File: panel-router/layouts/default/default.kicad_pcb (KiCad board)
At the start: 2 copper layers, 18.5 x 90 mm, 4 parts

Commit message: Cleanup
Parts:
- moved 15V-25V DC 19.8 mm to (93.0, 96.5), turned to 90 degrees
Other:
- outline, holes or cut-outs redrawn
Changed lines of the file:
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@@
 	(footprint "CUI_PJ_002BH:DC-IN-TH_PJ-002BH"
 		(layer "B.Cu")
-		(at 92.2048 116.2436)
+		(at 92.9525 96.495 90)
 		(property "Reference" "15V-25V DC"
-			(at 10.1572 4.4064 180)
-			(layer "B.SilkS")
-			(effects
-				(font
-					(size 1 1)
-					(thickness 0.15)
-				)
-				(justify left mirror)
+			(at 5.995 4.5475 90)
+			(layer "B.SilkS")
+			(effects
+				(font
+					(size 1 1)
+					(thickness 0.15)
+				)
+				(justify mirror)
 			)
 		)
 		(property "Value" ""
-			(at 0 -6.35 0)
+			(at 0 -6.35 90)
 			(layer "B.Fab")
 			(effects
@@
 		)
 		(property "Datasheet" "https://www.lcsc.com/datasheet/lcsc_datasheet_2409302136_CUI-PJ-002BH_C22359705.pdf"
-			(at 0 0 0)
+			(at 0 0 90)
 			(layer "User.9")
 			(hide yes)
@@
 		)
 		(property "Description" ""
-			(at 0 0 0)
+			(at 0 0 90)
 			(layer "B.Fab")
 			(hide yes)
@@
 		)
 		(property "LCSC" "C22359705"
-			(at 0 0 0)
+			(at 0 0 90)
 			(layer "User.9")
 			(hide yes)
@@
 		)
 		(property "Manufacturer" "CUI"
-			(at 0 0 0)
+			(at 0 0 90)
 			(layer "User.9")
 			(hide yes)
@@
 		)
 		(property "Partnumber" "PJ-002BH"
-			(at 0 0 0)
+			(at 0 0 90)
 			(layer "User.9")
 			(hide yes)
@@
 		)
 		(property "atopile_address" "dc_input"
-			(at 0 0 0)
+			(at 0 0 90)
 			(layer "User.9")
 			(hide yes)
@@
 		)
 		(property "lcsc_id" "C22359705"
-			(at 0 0 0)
+			(at 0 0 90)
 			(layer "User.9")
 			(hide yes)
@@
 		)
 		(attr through_hole)
+		(fp_line
+			(start 10.8 -6.98)
+			(end 10.8 2.29)
+			(stroke
+				(width 0.25)
+				(type solid)
+			)
+			(layer "B.SilkS")
+		)
 		(fp_line
 			(start -3.81 -6.98)
@@
 		)
 		(fp_line
+			(start 10.8 2.29)
+			(end 2.12 2.29)
+			(stroke
+				(width 0.25)
+				(type solid)
+			)
+			(layer "B.SilkS")
+		)
+		(fp_line
+			(start -2.12 2.29)
+			(end -3.81 2.29)
+			(stroke
+				(width 0.25)
+				(type solid)
+			)
+			(layer "B.SilkS")
+		)
+		(fp_line
 			(start -3.81 2.29)
 			(end -3.81 -0.33)
-			(stroke
-				(width 0.25)
-				(type solid)
-			)
-			(layer "B.SilkS")
-		)
-		(fp_line
-			(start -2.12 2.29)
-			(end -3.81 2.29)
-			(stroke
-				(width 0.25)
-				(type solid)
-			)
-			(layer "B.SilkS")
-		)
-		(fp_line
-			(start 10.8 -6.98)
-			(end 10.8 2.29)
-			(stroke
-				(width 0.25)
-				(type solid)
-			)
-			(layer "B.SilkS")
-		)
-		(fp_line
-			(start 10.8 2.29)
-			(end 2.12 2.29)
 			(stroke
 				(width 0.25)
@@
 		)
 		(pad "1" thru_hole oval
-			(at -3 -2.35)
+			(at -3 -2.35 90)
 			(size 1.7 4.3)
 			(drill oval 0.999998 3.499993)
@@
 		)
 		(pad "2" thru_hole oval
-			(at 3 -2.35)
+			(at 3 -2.35 90)
 			(size 1.7 3.8)
 			(drill oval 0.999998 2.999994)
@@
 		)
 		(pad "3" thru_hole oval
-			(at 0 2.35)
+			(at 0 2.35 90)
 			(size 3.8 1.7)
 			(drill oval 2.999994 0.999998)
@@
 		)
 	)
+	(gr_circle
+		(center 101.5 87)
+		(end 102.75 87)
+		(stroke
+			(width 0.05)
+			(type solid)
+		)
+		(fill no)
+		(layer "Edge.Cuts")
+	)
+	(gr_circle
+		(center 101.5 117)
+		(end 102.75 117)
+		(stroke
+			(width 0.05)
+			(type solid)
+		)
+		(fill no)
+		(layer "Edge.Cuts")
+	)
+	(gr_circle
+		(center 101.5 143)
+		(end 102.75 143)
+		(stroke
+			(width 0.05)
+			(type solid)
+		)
+		(fill no)
+		(layer "Edge.Cuts")
+	)
+	(gr_circle
+		(center 101.5 113)
+		(end 102.75 113)
+		(stroke
+			(width 0.05)
+			(type solid)
+		)
+		(fill no)
+		(layer "Edge.Cuts")
+	)
 	(gr_rect
 		(start 85 85)
@@
 		(stroke
 			(width 0.05)
+			(type solid)
+		)
+		(fill no)
+		(layer "Edge.Cuts")
+	)
+	(gr_circle
+		(center 101.5 173)
+		(end 102.75 173)
+		(stroke
+			(width 0.05)
+			(type solid)
+		)
+		(fill no)
+		(layer "Edge.Cuts")
+	)
+	(gr_circle
+		(center 101.5 147)
+		(end 102.75 147)
+		(stroke
+			(width 0.05)

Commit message: PoE Improvements
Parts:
- moved + H3 - 4.00 mm to (100.0, 164.0)
- moved 15V-25V DC 2.36 mm to (90.6, 96.4)
- moved + H2 - 2.00 mm to (100.0, 132.0)
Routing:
- net GND: track 0.00 -> 5.08 mm
- net V+: track 5.08 -> 7.62 mm
- net 4: track 75.9 -> 78.2 mm
- net 3: track 81.9 -> 83.2 mm
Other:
- board size 18.5 x 90 mm -> 21 x 94 mm
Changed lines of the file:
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@@
 	(footprint "BOOMELE_2_54_2_3P:HDR-TH_6P-P2.54-V-M-R2-C3-S2.54-1"
 		(layer "F.Cu")
-		(at 100 130 90)
+		(at 100 132 90)
 		(property "Reference" "+ H2 -"
 			(at 0 -4 90)
@@
 	(footprint "BOOMELE_2_54_2_3P:HDR-TH_6P-P2.54-V-M-R2-C3-S2.54-1"
 		(layer "F.Cu")
-		(at 100 160 90)
+		(at 100 164 90)
 		(property "Reference" "+ H3 -"
 			(at 0 -4 90)
@@
 	(footprint "CUI_PJ_002BH:DC-IN-TH_PJ-002BH"
 		(layer "B.Cu")
-		(at 92.9525 96.495 90)
+		(at 90.5896 96.4212 90)
 		(property "Reference" "15V-25V DC"
 			(at 5.995 4.5475 90)
@@
 	)
 	(gr_circle
-		(center 101.5 117)
-		(end 102.75 117)
+		(center 101.5 119)
+		(end 102.75 119)
 		(stroke
 			(width 0.05)
@@
 	)
 	(gr_circle
-		(center 101.5 143)
-		(end 102.75 143)
+		(center 101.5 145)
+		(end 102.75 145)
 		(stroke
 			(width 0.05)
@@
 	)
 	(gr_rect
-		(start 85 85)
-		(end 103.5 175)
+		(start 82.5 85)
+		(end 103.5 179)
 		(stroke
 			(width 0.05)
@@
 	)
 	(gr_circle
-		(center 101.5 173)
-		(end 102.75 173)
+		(center 101.5 177)
+		(end 102.75 177)
 		(stroke
 			(width 0.05)
@@
 	)
 	(gr_circle
-		(center 101.5 147)
-		(end 102.75 147)
+		(center 101.5 151)
+		(end 102.75 151)
 		(stroke
 			(width 0.05)
@@
 	)
 	(segment
-		(start 98.73 162.54)
-		(end 101.27 162.54)
-		(width 0.4)
-		(layer "F.Cu")
+		(start 98.73 161.46)
+		(end 101.27 161.46)
+		(width 0.5)
+		(layer "F.Cu")
+		(net 1)
+	)
+	(segment
+		(start 98.73 97.46)
+		(end 101.27 97.46)
+		(width 0.5)
+		(layer "F.Cu")
+		(net 1)
+	)
+	(segment
+		(start 101.27 102.54)
+		(end 98.73 102.54)
+		(width 0.5)
+		(layer "B.Cu")
 		(net 2)
 	)
 	(segment
-		(start 98.73 132.54)
-		(end 101.27 132.54)
-		(width 0.4)
-		(layer "F.Cu")
+		(start 98.73 134.54)
+		(end 101.27 134.54)
+		(width 0.5)
+		(layer "B.Cu")
 		(net 2)
 	)
 	(segment
-		(start 92.9132 128.7272)
-		(end 92.8116 128.6256)
-		(width 0.2)
-		(layer "F.Cu")
-		(net 3)
-	)
-	(segment
-		(start 96.4184 158.6992)
-		(end 99.9692 158.6992)
-		(width 0.2)
-		(layer "F.Cu")
-		(net 3)
-	)
-	(segment
-		(start 101.1964 130)
-		(end 99.9236 128.7272)
+		(start 98.73 166.54)
+		(end 101.27 166.54)
+		(width 0.5)
+		(layer "B.Cu")
+		(net 2)
+	)
+	(segment
+		(start 92.8116 128.6256)
+		(end 92.8116 124.5108)
+		(width 0.2)
+		(layer "F.Cu")
+		(net 3)
+	)
+	(segment
+		(start 97.536 162.7632)
+		(end 100.0332 162.7632)
 		(width 0.2)
 		(layer "F.Cu")
@@
 	)
 	(segment
+		(start 92.8116 124.5108)
+		(end 98.9584 118.364)
+		(width 0.2)
+		(layer "F.Cu")
+		(net 3)
+	)
+	(segment
+		(start 100.0292 130.7592)
+		(end 101.27 132)
+		(width 0.2)
+		(layer "F.Cu")
+		(net 3)
+	)
+	(segment
+		(start 94.8944 130.7592)
+		(end 94.7928 130.6576)
+		(width 0.2)
+		(layer "F.Cu")
+		(net 3)
+	)
+	(segment
+		(start 95.8596 161.0868)
+		(end 97.536 162.7632)
+		(width 0.2)
+		(layer "F.Cu")
+		(net 3)
+	)
+	(segment
+		(start 100.0332 162.7632)
+		(end 101.27 164)
+		(width 0.2)
+		(layer "F.Cu")
+		(net 3)
+	)
+	(segment
+		(start 94.7928 130.6576)
+		(end 94.7928 130.6068)
+		(width 0.2)
+		(layer "F.Cu")
+		(net 3)
+	)
+	(segment
 		(start 95.8596 149.352)
-		(end 95.8596 158.1404)
-		(width 0.2)
-		(layer "F.Cu")
-		(net 3)
-	)
-	(segment
-		(start 101.27 130)
-		(end 101.1964 130)
+		(end 95.8596 161.0868)
+		(width 0.2)
+		(layer "F.Cu")
+		(net 3)
+	)
+	(segment
+		(start 94.8944 130.7592)
+		(end 100.0292 130.7592)
 		(width 0.2)
 		(layer "F.Cu")
@@
 	)
 	(segment
-		(start 99.9692 158.6992)
-		(end 101.27 160)
-		(width 0.2)
-		(layer "F.Cu")
-		(net 3)
-	)
-	(segment
-		(start 95.8596 158.1404)
-		(end 96.4184 158.6992)
-		(width 0.2)
-		(layer "F.Cu")
-		(net 3)
-	)
-	(segment
-		(start 99.9236 128.7272)
-		(end 92.9132 128.7272)
-		(width 0.2)
-		(layer "F.Cu")
-		(net 3)
-	)
-	(segment
-		(start 92.8116 124.5108)
-		(end 98.9584 118.364)
-		(width 0.2)
-		(layer "F.Cu")
-		(net 3)
-	)
-	(segment
-		(start 92.8116 128.6256)
-		(end 92.8116 124.5108)
+		(start 94.7928 130.6068)
+		(end 92.8116 128.6256)
 		(width 0.2)
 		(layer "F.Cu")
@@
 	)
 	(via
-		(at 92.8116 128.6256)
+		(at 94.8944 130.7592)
 		(size 0.6)
 		(drill 0.3)
@@
 	)
 	(segment
+		(start 94.7928 148.2852)
+		(end 95.8596 149.352)
+		(width 0.2)
+		(layer "B.Cu")
+		(net 3)
+	)
+	(segment
 		(start 100.0256 101.2444)
 		(end 101.27 100)
@@
 	)
 	(segment
-		(start 94.7928 148.2852)
-		(end 95.8596 149.352)
-		(width 0.2)
-		(layer "B.Cu")
-		(net 3)
-	)
-	(segment
 		(start 96.4184 101.9556)
 		(end 97.1296 101.2444)
@@
 	)
 	(segment
-		(start 94.7928 130.6068)
-		(end 94.7928 148.2852)
+		(start 94.8944 130.7592)
+		(end 94.7928 130.8608)
 		(width 0.2)
 		(layer "B.Cu")
@@
 	)
 	(segment
-		(start 92.8116 128.6256)
-		(end 94.7928 130.6068)
-		(width 0.2)
-		(layer "B.Cu")
-		(net 3)
-	)
-	(segment
-		(start 96.012 159.1056)
-		(end 97.8356 159.1056)
+		(start 94.7928 130.8608)
+		(end 94.7928 148.2852)
+		(width 0.2)
+		(layer "B.Cu")
+		(net 3)
+	)
+	(segment
+		(start 92.1004 124.0536)
+		(end 98.1964 117.9576)
+		(width 0.2)
+		(layer "F.Cu")
+		(net 4)
+	)
+	(segment
+		(start 98.3528 131.6228)
+		(end 98.73 132)
 		(width 0.2)
 		(layer "F.Cu")
@@
 	(segment
 		(start 95.1484 149.5552)
-		(end 95.1484 158.242)
-		(width 0.2)
-		(layer "F.Cu")
-		(net 4)
-	)
-	(segment
-		(start 97.8356 159.1056)
-		(end 98.73 160)
+		(end 95.1484 162.1536)
+		(width 0.2)
+		(layer "F.Cu")
+		(net 4)
+	)
+	(segment
+		(start 94.0308 131.6228)
+		(end 92.1004 129.6924)
+		(width 0.2)
+		(layer "F.Cu")
+		(net 4)
+	)
+	(segment
+		(start 94.0308 148.4376)
+		(end 95.1484 149.5552)
+		(width 0.2)
+		(layer "F.Cu")
+		(net 4)
+	)
+	(segment
+		(start 98.1964 117.9576)
+		(end 98.1964 109.5248)
+		(width 0.2)
+		(layer "F.Cu")
+		(net 4)
+	)
+	(segment
+		(start 96.9948 164)
+		(end 98.73 164)
+		(width 0.2)
+		(layer "F.Cu")
+		(net 4)
+	)
+	(segment
+		(start 94.0308 131.6228)
+		(end 98.3528 131.6228)
+		(width 0.2)
+		(layer "F.Cu")
+		(net 4)
+	)
+	(segment
+		(start 95.1484 162.1536)
+		(end 96.9948 164)
 		(width 0.2)
 		(layer "F.Cu")
@@
 		(net 4)
 	)
-	(segment
-		(start 92.254 129.846)
-		(end 92.408 130)
-		(width 0.2)
-		(layer "F.Cu")
-		(net 4)
-	)
-	(segment
-		(start 98.1964 117.9576)
-		(end 98.1964 109.5248)
-		(width 0.2)
-		(layer "F.Cu")
-		(net 4)
-	)
-	(segment
-		(start 92.408 130)
-		(end 98.73 130)
-		(width 0.2)
-		(layer "F.Cu")
-		(net 4)
-	)
-	(segment
-		(start 92.1004 124.0536)
-		(end 98.1964 117.9576)
-		(width 0.2)
-		(layer "F.Cu")
-		(net 4)
-	)
-	(segment
-		(start 92.254 129.846)
-		(end 92.1004 129.6924)
-		(width 0.2)
-		(layer "F.Cu")
-		(net 4)
-	)
-	(segment
-		(start 95.1484 158.242)
-		(end 96.012 159.1056)
-		(width 0.2)
-		(layer "F.Cu")
-		(net 4)
-	)
-	(segment
-		(start 94.0308 148.4376)
-		(end 95.1484 149.5552)
-		(width 0.2)
-		(layer "F.Cu")
-		(net 4)
-	)
 	(via
-		(at 92.254 129.846)
+		(at 94.0308 131.6228)
 		(size 0.6)
 		(drill 0.3)
@@
 	)
 	(segment
-		(start 92.254 129.846)
-		(end 94.0308 131.6228)
+		(start 98.1964 108.1024)
+		(end 95.8088 105.7148)
 		(width 0.2)
 		(layer "B.Cu")
@@
 		(start 94.0308 131.6228)
 		(end 94.0308 148.4376)
-		(width 0.2)
-		(layer "B.Cu")
-		(net 4)
-	)
-	(segment
-		(start 98.1964 108.1024)
-		(end 95.8088 105.7148)
 		(width 0.2)
 		(layer "B.Cu")
@@
 		(polygon
 			(pts
-				(xy 76.1524 80.9364) (xy 111.1524 80.9364) (xy 110.5936 177.6708) (xy 75.5936 177.6708)
+				(xy 76.1524 80.9364) (xy 111.1524 80.9364) (xy 110.7968 180.5664) (xy 75.7968 180.5664)
 			)
 		)
@@
 		(polygon
 			(pts
-				(xy 80.7112 83.330902) (xy 115.7112 83.330902) (xy 115.6096 178.846102) (xy 80.6096 178.846102)
-			)
-		)
+				(xy 80.7112 83.330902) (xy 115.7112 83.330902) (xy 115.7112 182.249702) (xy 80.7112 182.249702)
+			)
+		)

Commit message: Header & Silkscreen Updates
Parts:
- H1: renamed from + H1 -
- H2: renamed from + H2 -
- H3: renamed from + H3 -
- moved H1 15.5 mm to (96.0, 115.0), turned to -90 degrees
- moved H2 15.5 mm to (96.0, 147.0), turned to -90 degrees
- moved H3 15.5 mm to (96.0, 179.0), turned to -90 degrees
- moved 15V-25V DC 15.4 mm to (87.1, 111.4)
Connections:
- H1 pad 2: V+ -> GND
- H1 pad 5: GND -> V+
- H2 pad 2: V+ -> GND
- H2 pad 5: GND -> V+
- H3 pad 2: V+ -> GND
- H3 pad 5: GND -> V+
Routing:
- net V+: track 7.62 -> 0.00 mm
- net 4: track 78.2 -> 83.8 mm
- net GND: track 5.08 -> 0.00 mm
- net 3: track 83.2 -> 78.2 mm

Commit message: Basic layout tweaks
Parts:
- moved H3 2.00 mm to (96.0, 177.0)
- moved H2 1.00 mm to (96.0, 146.0)
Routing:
- net 4: track 83.8 -> 81.3 mm
- net 3: track 78.2 -> 77.2 mm
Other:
- board size 21 x 94 mm -> 21 x 92 mm
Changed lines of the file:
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@@
 	(footprint "BOOMELE_2_54_2_3P:HDR-TH_6P-P2.54-V-M-R2-C3-S2.54-1"
 		(layer "F.Cu")
-		(at 96 147 -90)
+		(at 96 146 -90)
 		(property "Reference" "H2"
 			(at 0 3.5 90)
@@
 	(footprint "BOOMELE_2_54_2_3P:HDR-TH_6P-P2.54-V-M-R2-C3-S2.54-1"
 		(layer "F.Cu")
-		(at 96 179 -90)
+		(at 96 177 -90)
 		(property "Reference" "H3"
 			(at 0 3.5 90)
@@
 	)
 	(gr_circle
-		(center 98 134)
-		(end 99.25 134)
+		(center 98 133)
+		(end 99.25 133)
 		(stroke
 			(width 0.05)
@@
 	)
 	(gr_circle
-		(center 98 160)
-		(end 99.25 160)
+		(center 98 159)
+		(end 99.25 159)
 		(stroke
 			(width 0.05)
@@
 	(gr_rect
 		(start 79 100)
-		(end 100 194)
+		(end 100 192)
 		(stroke
 			(width 0.05)
@@
 	)
 	(gr_circle
-		(center 98 192)
-		(end 99.25 192)
+		(center 98 190)
+		(end 99.25 190)
 		(stroke
 			(width 0.05)
@@
 	)
 	(gr_circle
-		(center 98 166)
-		(end 99.25 166)
+		(center 98 164)
+		(end 99.25 164)
 		(stroke
 			(width 0.05)
@@
 	)
 	(segment
-		(start 94.8528 146.6228)
-		(end 95.23 147)
-		(width 0.2)
-		(layer "F.Cu")
-		(net 1)
-	)
-	(segment
 		(start 90.5308 146.6228)
 		(end 88.6004 144.6924)
@@
 	)
 	(segment
+		(start 94.73 177)
+		(end 95.23 177.5)
+		(width 0.2)
+		(layer "F.Cu")
+		(net 1)
+	)
+	(segment
 		(start 90.5764 163.4832)
 		(end 90.5764 176.0816)
@@
 	)
 	(segment
+		(start 90.5308 146.6228)
+		(end 90.6536 146.5)
+		(width 0.2)
+		(layer "F.Cu")
+		(net 1)
+	)
+	(segment
+		(start 94.6964 132.9576)
+		(end 94.6964 124.5248)
+		(width 0.2)
+		(layer "F.Cu")
+		(net 1)
+	)
+	(segment
+		(start 94.23 146.5)
+		(end 94.73 146)
+		(width 0.2)
+		(layer "F.Cu")
+		(net 1)
+	)
+	(segment
 		(start 90.5308 163.4376)
 		(end 90.5764 163.4832)
@@
 	)
 	(segment
-		(start 94.6964 132.9576)
-		(end 94.6964 124.5248)
-		(width 0.2)
-		(layer "F.Cu")
-		(net 1)
-	)
-	(segment
-		(start 93.4948 179)
-		(end 95.23 179)
-		(width 0.2)
-		(layer "F.Cu")
-		(net 1)
-	)
-	(segment
-		(start 90.5308 146.6228)
-		(end 94.8528 146.6228)
-		(width 0.2)
-		(layer "F.Cu")
-		(net 1)
-	)
-	(segment
 		(start 90.5764 176.0816)
-		(end 93.4948 179)
+		(end 91.4948 177)
+		(width 0.2)
+		(layer "F.Cu")
+		(net 1)
+	)
+	(segment
+		(start 91.4948 177)
+		(end 94.73 177)
+		(width 0.2)
+		(layer "F.Cu")
+		(net 1)
+	)
+	(segment
+		(start 90.6536 146.5)
+		(end 94.23 146.5)
 		(width 0.2)
 		(layer "F.Cu")
@@
 	)
 	(segment
+		(start 96.77 146)
+		(end 97.27 146)
+		(width 0.2)
+		(layer "F.Cu")
+		(net 2)
+	)
+	(segment
 		(start 89.3116 143.6256)
 		(end 89.3116 139.5108)
@@
 	)
 	(segment
+		(start 91.2368 173.9868)
+		(end 93 175.75)
+		(width 0.2)
+		(layer "F.Cu")
+		(net 2)
+	)
+	(segment
 		(start 95.4584 133.364)
 		(end 95.4584 122.7468)
@@
 	)
 	(segment
-		(start 96.5332 177.7632)
-		(end 97.77 179)
+		(start 96.02 175.75)
+		(end 97.27 177)
 		(width 0.2)
 		(layer "F.Cu")
@@
 	)
 	(segment
-		(start 93.1304 177.7632)
-		(end 96.5332 177.7632)
+		(start 92.4036 144.75)
+		(end 95.52 144.75)
 		(width 0.2)
 		(layer "F.Cu")
@@
 	)
 	(segment
-		(start 96.5292 145.7592)
-		(end 97.77 147)
+		(start 91.3944 145.7592)
+		(end 92.4036 144.75)
 		(width 0.2)
 		(layer "F.Cu")
@@
 	)
 	(segment
-		(start 91.2368 175.8696)
-		(end 93.1304 177.7632)
-		(width 0.2)
-		(layer "F.Cu")
-		(net 2)
-	)
-	(segment
 		(start 91.2928 145.6576)
 		(end 91.2928 145.6068)
@@
 	)
 	(segment
+		(start 95.52 144.75)
+		(end 96.77 146)
+		(width 0.2)
+		(layer "F.Cu")
+		(net 2)
+	)
+	(segment
 		(start 91.2368 164.8968)
-		(end 91.2368 175.8696)
-		(width 0.2)
-		(layer "F.Cu")
-		(net 2)
-	)
-	(segment
-		(start 91.3944 145.7592)
-		(end 96.5292 145.7592)
+		(end 91.2368 173.9868)
 		(width 0.2)
 		(layer "F.Cu")
@@
 		(width 0.2)
 		(layer "F.Cu")
+		(net 2)
+	)
+	(segment
+		(start 93 175.75)
+		(end 96.02 175.75)
+		(width 0.2)
+		(layer "F.Cu")

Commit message: Finishing up panel-router
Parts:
- added QR*****: LED-GitHub-QR-MD, Silkscreen:LED-GitHub-QR-MD, B.Cu at (86.6, 184.3)
- added REF**: OSHW-Logo2_7.3x6mm_SilkScreen, Symbol:OSHW-Logo2_7.3x6mm_SilkScreen, B.Cu at (86.6, 173.5)
- added REF**: KiCad-Logo2_5mm_SilkScreen, Symbol:KiCad-Logo2_5mm_SilkScreen, B.Cu at (86.6, 161.0)
- added TP_COOL: TestPoint_Pad_D1.0mm, TestPoint_Pad_D1_0mm:TestPoint_Pad_D1.0mm, F.Cu at (94.5, 124.6)
- added TP_GND: TestPoint_Pad_D1.0mm, TestPoint_Pad_D1_0mm:TestPoint_Pad_D1.0mm, F.Cu at (97.2, 109.2)
- added TP_V+: TestPoint_Pad_D1.0mm, TestPoint_Pad_D1_0mm:TestPoint_Pad_D1.0mm, F.Cu at (93.7, 106.6)
- added TP_WARM: TestPoint_Pad_D1.0mm, TestPoint_Pad_D1_0mm:TestPoint_Pad_D1.0mm, F.Cu at (95.5, 122.7)
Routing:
- net GND: track 0.00 -> 3.51 mm
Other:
- board text added: "Panel Router v1.0.2 - June 2026"

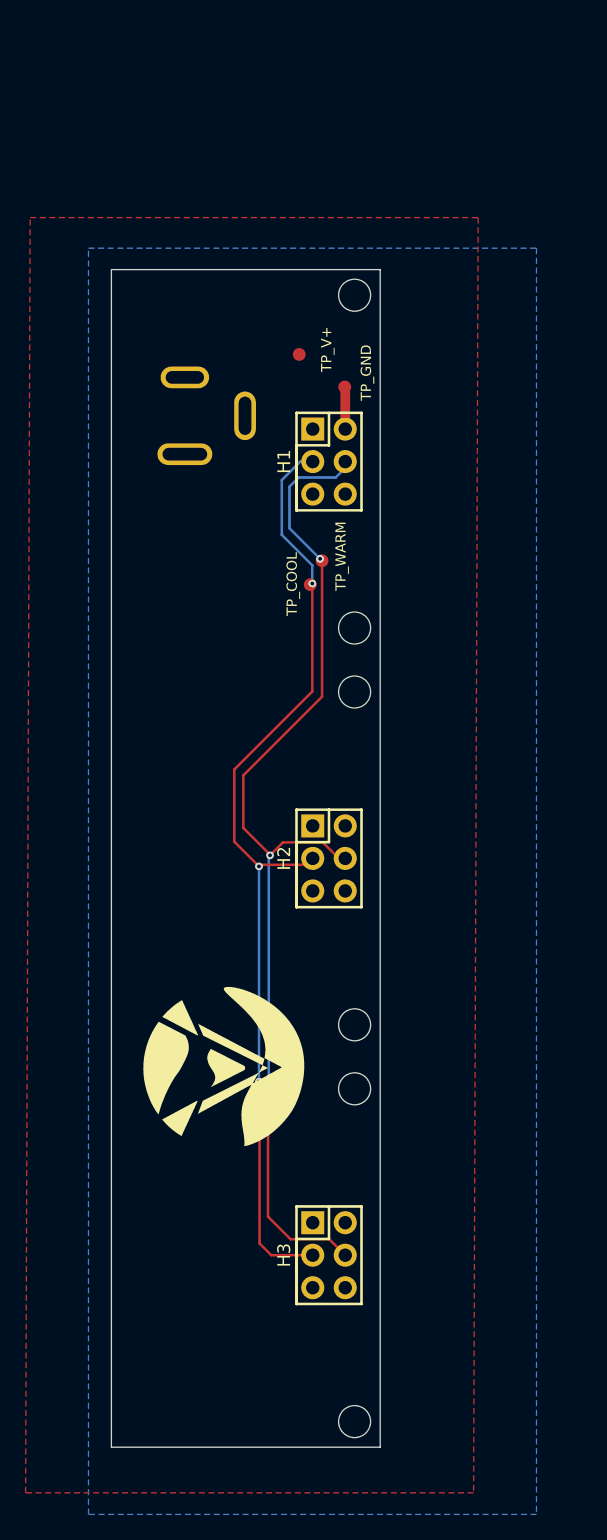
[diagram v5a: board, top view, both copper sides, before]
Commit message: Fixed 3D offsets, flipped some DC jacks, and added screw holes
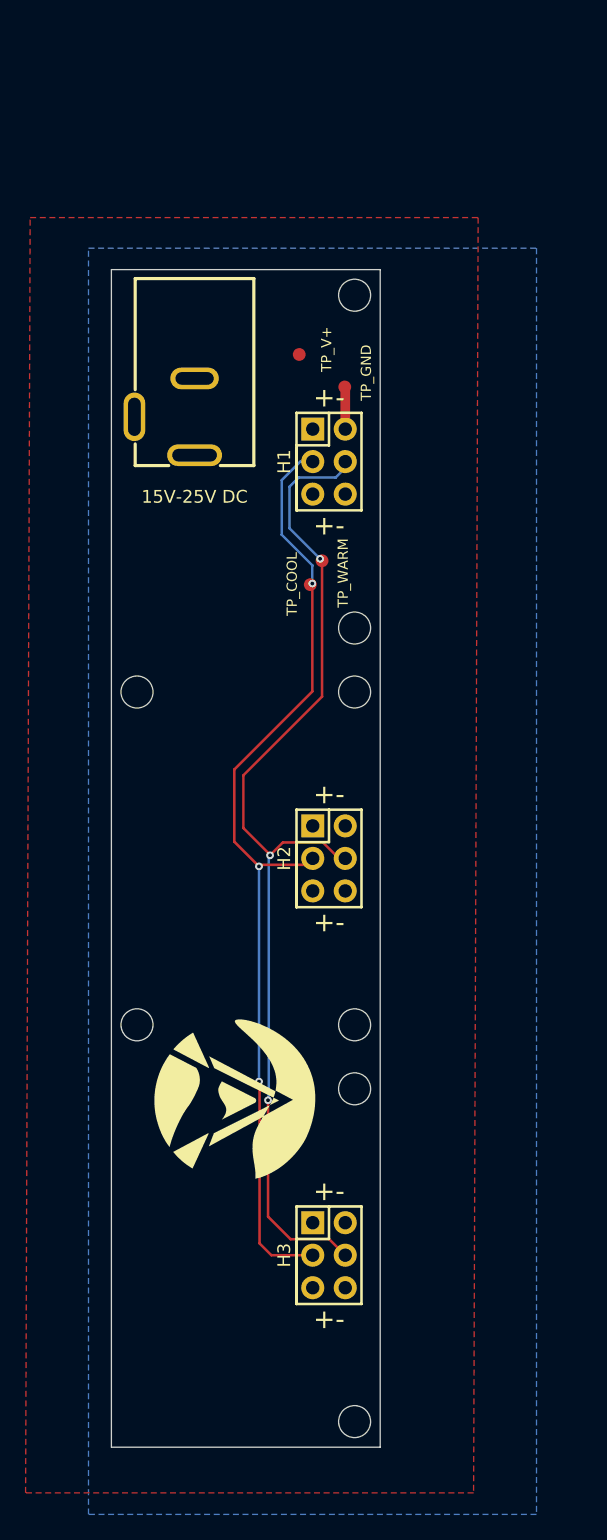
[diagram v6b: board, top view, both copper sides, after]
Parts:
- 15V-25V DC: moved to F.Cu
- moved 15V-25V DC 3.94 mm to (83.2, 111.5)
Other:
- outline, holes or cut-outs redrawn
- board text added: "+-"
- board text added: "Panel Router v1.0.3 - June 2026"
- board text removed: "Panel Router v1.0.2 - June 2026"
